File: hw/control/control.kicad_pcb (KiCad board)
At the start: 2 copper layers, 200 x 90 mm, 143 parts, among them J101 Screw_Terminal_01x02, J102 Screw_Terminal_01x03, J103 Screw_Terminal_01x03, J301 Conn_02x05_Odd_Even, J302 Conn_01x04, J303 Raspberry_Pi_0_2_3, J304 Micro_SD_Card, J305 Conn_01x06, Q1001 BC807, Q1002 BC817, Q401 BC817, Q501 BC817, Q601 BC817, Q701 BC817, Q801 BC807, Q802 BC817, Q901 AOSP21357, Q902 IRF4905, U1001 LM2678T-ADJ, U1101 SN74AHCT125D, U201 LM2596T-ADJ, U801 LM2678T-ADJ

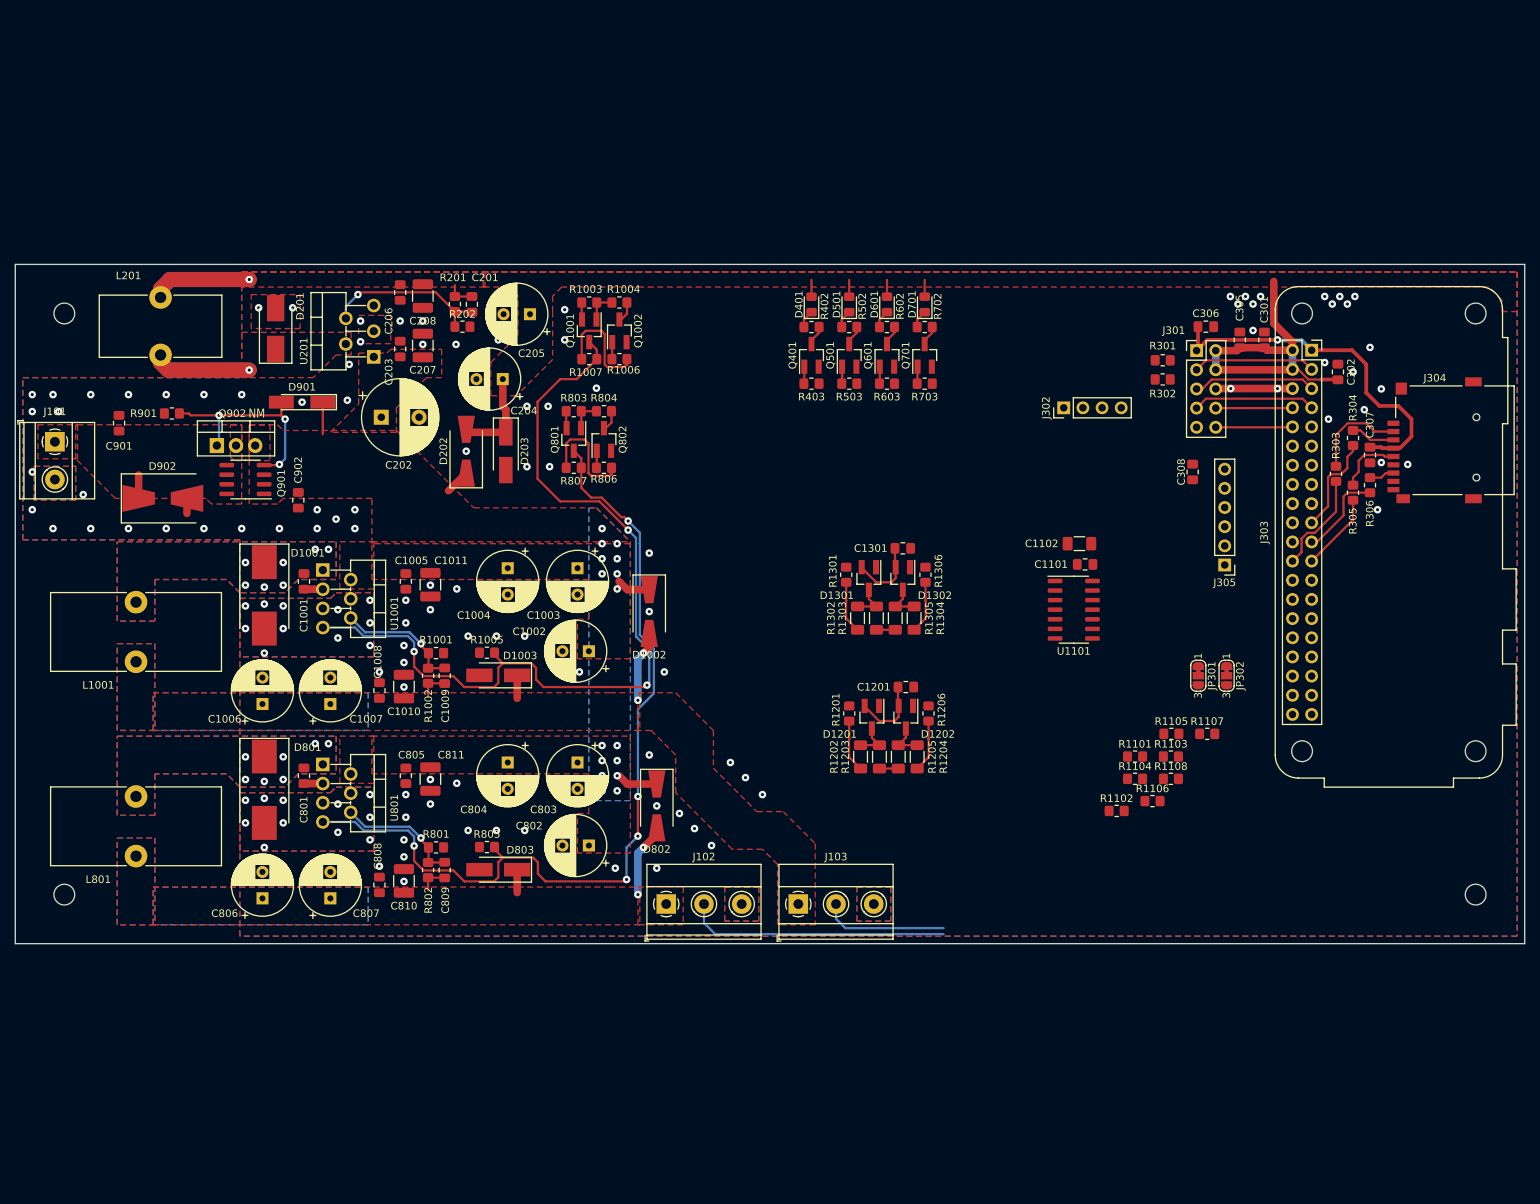
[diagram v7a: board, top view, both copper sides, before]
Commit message: [hw] Reduce size of the control PCB
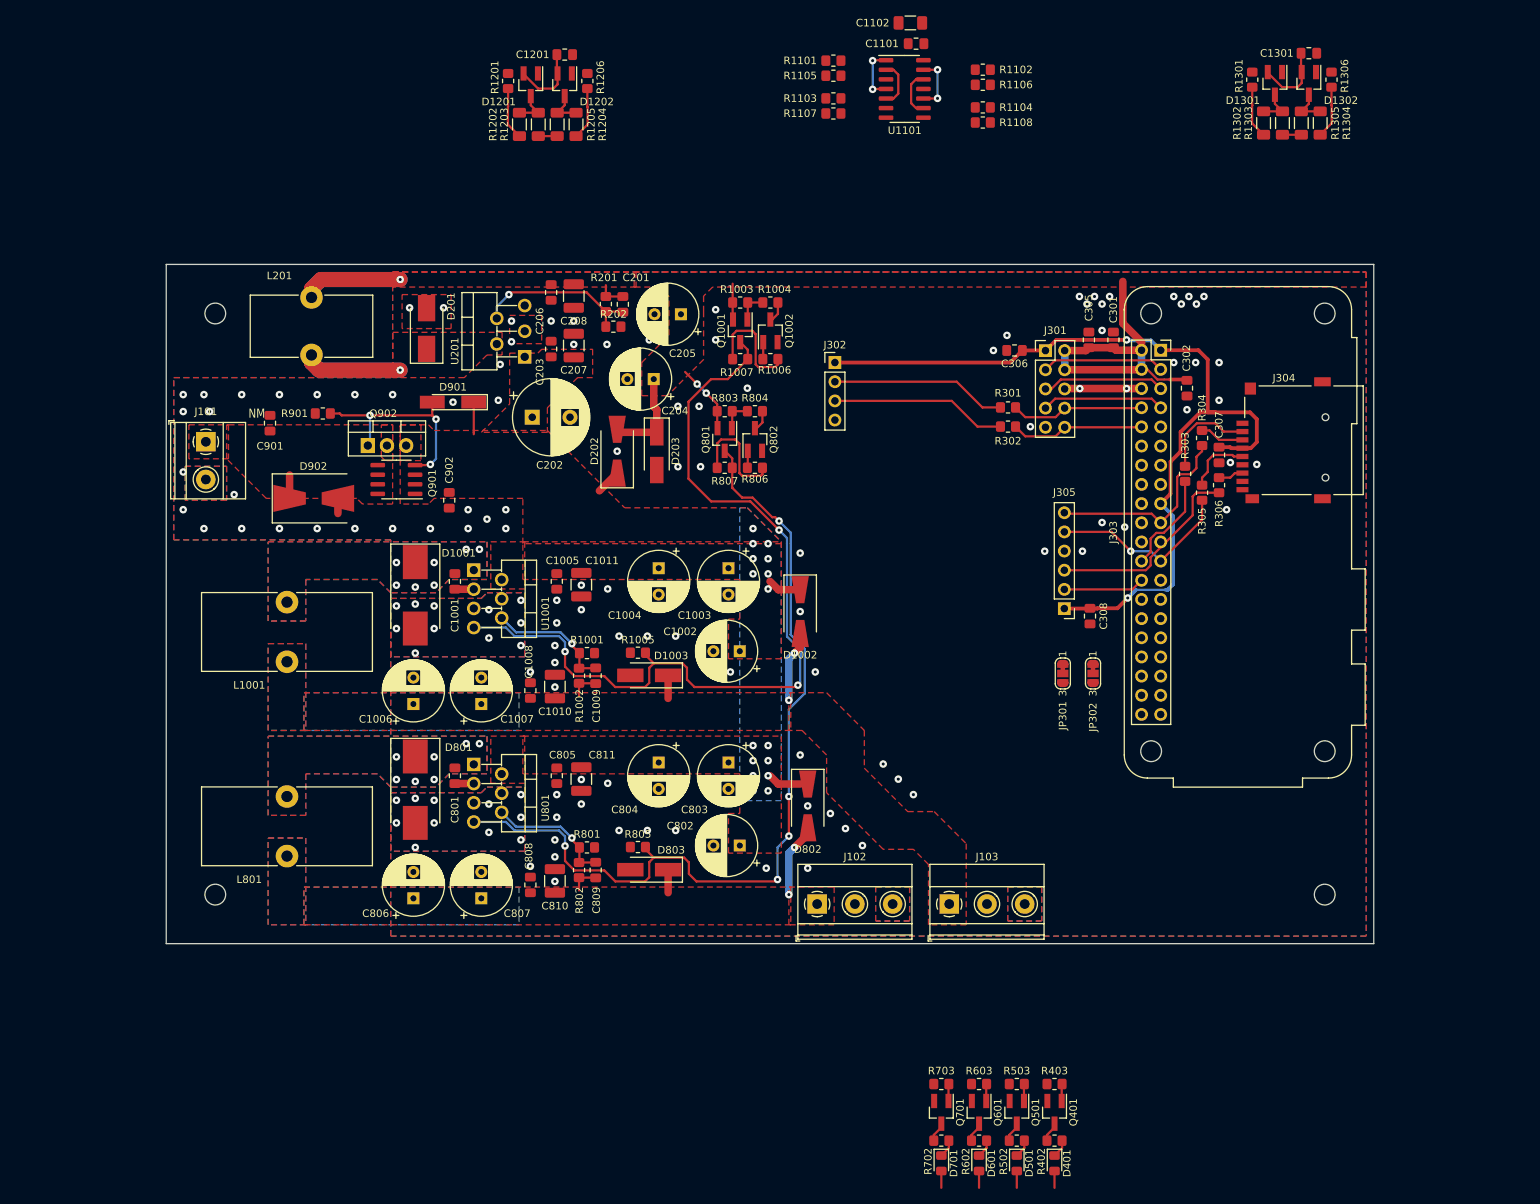
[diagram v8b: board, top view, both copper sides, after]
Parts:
- moved D401 118.3 mm to (177.7, 169.1), turned to 270 degrees
- moved D501 115.9 mm to (172.7, 169.1), turned to 270 degrees
- moved D601 114.5 mm to (167.7, 169.1), turned to 270 degrees
- moved D701 113.8 mm to (162.7, 169.1), turned to 270 degrees
- moved R402 112.5 mm to (177.7, 166.1), turned to 180 degrees
- moved R502 110.1 mm to (172.7, 166.1), turned to 180 degrees
- moved R602 108.5 mm to (167.7, 166.1), turned to 180 degrees
- moved R702 107.8 mm to (162.7, 166.1), turned to 180 degrees
- moved Q401 105.3 mm to (177.7, 162.3), turned to 270 degrees
- moved Q501 102.7 mm to (172.7, 162.3), turned to 270 degrees
- moved Q601 101.0 mm to (167.7, 162.3), turned to 270 degrees
- moved R1101 100.5 mm to (148.4, 23.0), turned to 180 degrees
- moved Q701 100.3 mm to (162.7, 162.3), turned to 270 degrees
- moved R1102 99.8 mm to (168.2, 24.2)
- moved R403 98.2 mm to (177.7, 158.6), turned to 180 degrees
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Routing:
- net +3V3: track 47.9 -> 118.2 mm, vias 1 -> 2
- net /LED Driver/DATA_OUT0: track 37.4 -> 2.50 mm
- net Net-(J302-Pad3): track 0.00 -> 23.3 mm
- net Net-(J302-Pad2): track 0.00 -> 23.3 mm
- net /LED Driver/DATA_OUT1: track 19.2 -> 2.50 mm
- net /CPU/SPI0_MISO: track 11.9 -> 27.3 mm
- net /CPU/SPI0_CLK: track 10.3 -> 24.7 mm, vias 0 -> 1
- net /CPU/SPI0_MOSI: track 13.3 -> 26.6 mm
- net /CPU/SPI0_CS1: track 0.00 -> 10.7 mm
- net +5V: track 118.9 -> 128.3 mm, vias 1 -> 3
- net Net-(R1102-Pad1): track 0.00 -> 7.56 mm, vias 0 -> 2
- net /CPU/UART_TXD: track 10.2 -> 17.7 mm
- net /CPU/UART_RXD: track 10.2 -> 17.7 mm
- net Net-(R1101-Pad1): track 0.00 -> 7.40 mm, vias 0 -> 2
- net Net-(R1103-Pad2): track 0.00 -> 6.30 mm
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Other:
- board size 200 x 90 mm -> 160 x 90 mm
